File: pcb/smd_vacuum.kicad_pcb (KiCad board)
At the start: 2 copper layers, 71 x 72.4 mm, 32 parts, among them J1 PWR, M1 Motor_DC, Q1 IRF5305, Q2 Q_NMOS_GDS, Q3 Q_NMOS_GDS, SW1 SW_SPST, U1 NE555P, U2 EL817

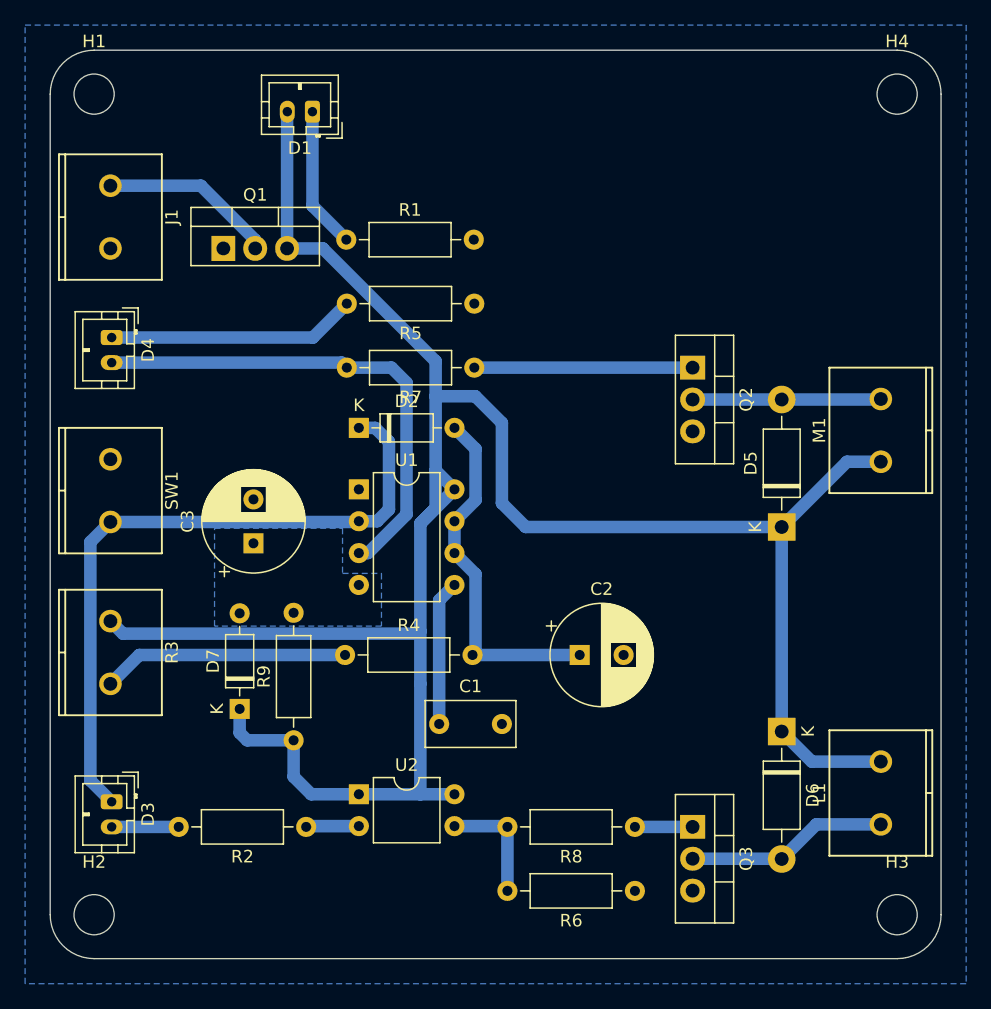
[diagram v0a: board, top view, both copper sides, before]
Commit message: to new kicad version
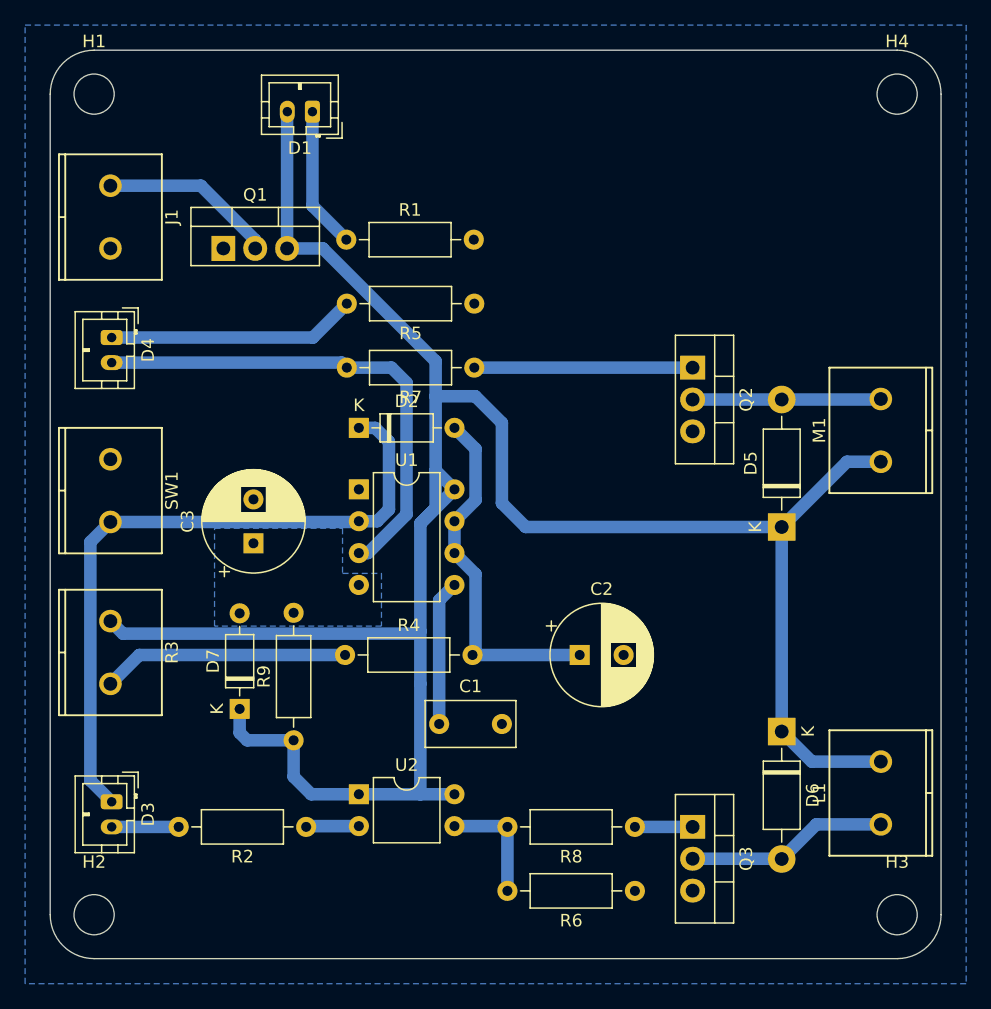
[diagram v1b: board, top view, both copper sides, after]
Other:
- net class Default removed
